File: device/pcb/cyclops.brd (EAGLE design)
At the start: 124.5 x 79.9 mm, 187 parts, among them Q1 SSM3K324, Q2 SSM3K324, Q3 SSM3K324, Q4 IRF510, U1 MCP4921, U10 ADG1201, U11 THS4281, U12 MAX4564, U13 ZXTD, U14 ZXTD, U15 OPA1664, U16 LTM8020, U2 LT1931, U3 LT1764A, U4 BD00FC0WEFJ, U5 TPS72325, U6 LT1711, U7 TLV3701, U8 ADR03, U9 LT1880

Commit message: Towards final updates for revision 3.6
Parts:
- removed D1: 1N5819, jonnew:SOD123
- added VREF<>TTL1: AS12CV, jonnew:AS12A*_SPDT
- Q1, Q2: value SSM3K324 -> NDS351AN
- U69: value SSM3K324 -> FDN352AP
- renumbered Q3 to U69
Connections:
- net OVER_CURR_PRE renamed ~OVER_CURR_PRE
- removed net OC: OC.C2, U69.D
- removed net OVER_CURR: U10.6
- new net N$16: R30.2, U69.D
- new net N$19: VCTL.1, VREF<>TTL1.P1
- net +6V: now also R29.1, U69.S; no longer R30.2
- net GND: now also OC.C2; no longer R29.1, U69.S
- net REF5.0: now also VREF<>TTL1.P3
- net VINPUT: now also VREF<>TTL1.P2; no longer VCTL.1
- net ~OVER_CURR: now also U10.6
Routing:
- net ~OVER_CURR: track 0.00 -> 18.8 mm, vias 0 -> 2
- net OVER_CURR: track 15.4 -> 0.00 mm, vias 2 -> 0
- net REF5.0: track 71.2 -> 84.3 mm
- net OC: track 12.0 -> 0.00 mm
- net N$19: track 0.00 -> 8.52 mm
- net VINPUT: track 59.3 -> 66.8 mm, vias 0 -> 1
- net GND: track 107.1 -> 104.5 mm, vias 419 -> 418
- net N$16: track 0.00 -> 2.55 mm
- net LED_ACTIVE: track 77.3 -> 75.3 mm, vias 4 -> 2
- net +6V: track 59.7 -> 61.3 mm
- net VAUX_OUT: track 46.7 -> 45.9 mm, vias 4 -> 2
- net VI: vias 2 -> 0
- net N$37: vias 0 -> 2
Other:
- board text added: "VCTL or CONT"
- board text added: "VREF or LED_ACTIVE"

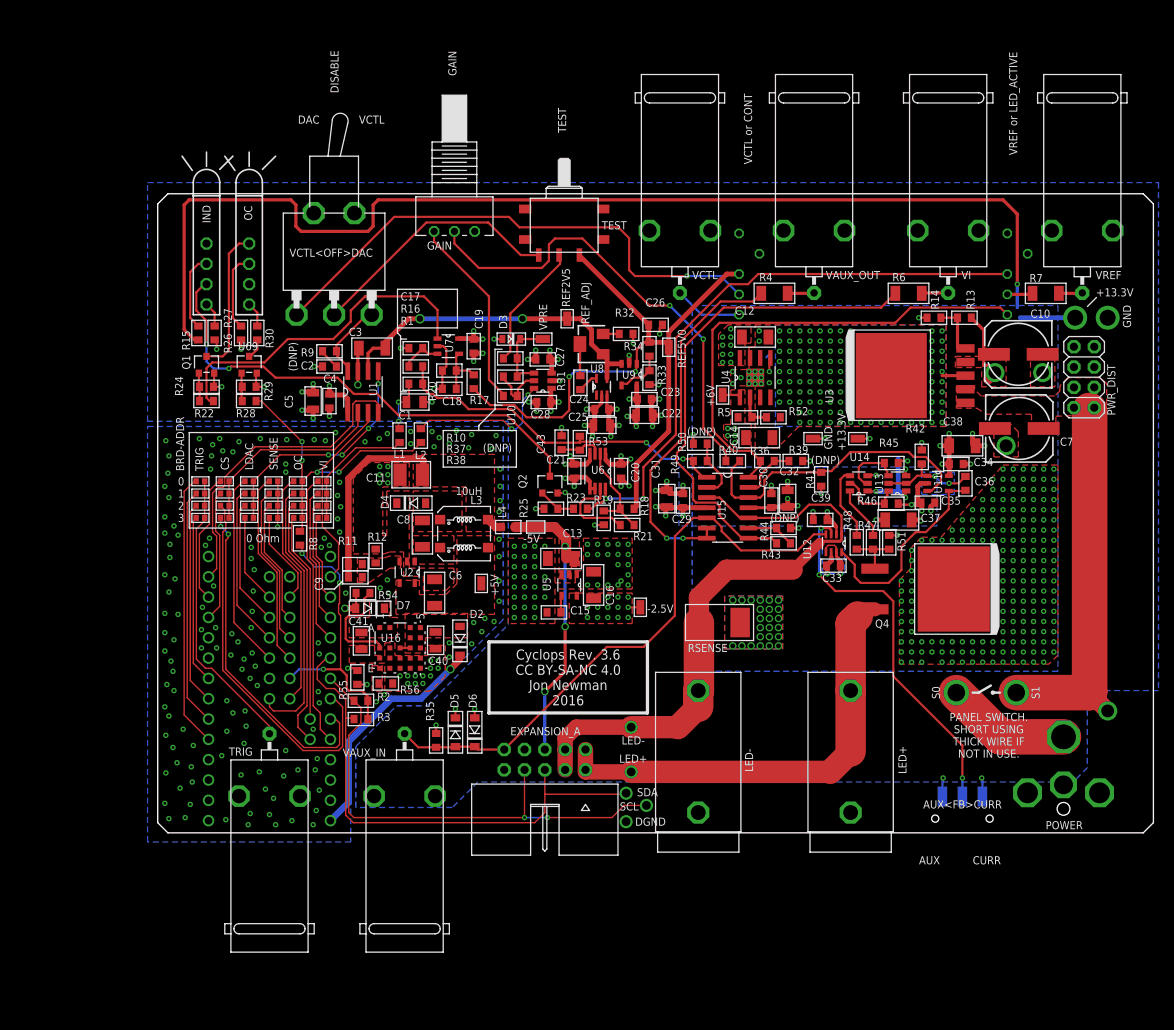
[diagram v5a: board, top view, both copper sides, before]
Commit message: Moved the LED to drain side of FET
- This prevents Vgs from dropping in nonlinear fashion as LED turns on.
  Not sure why LED was on low side to begin with.
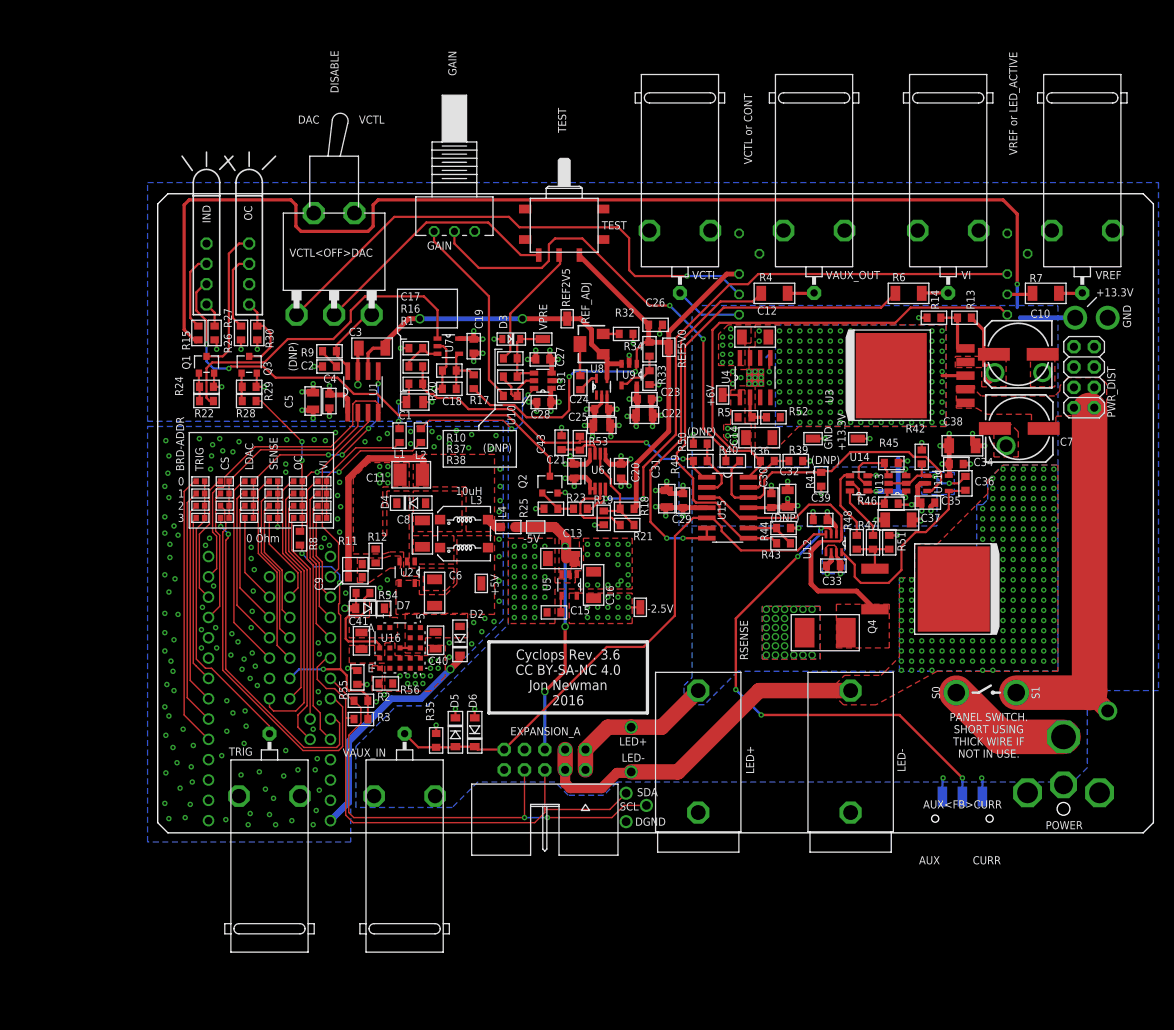
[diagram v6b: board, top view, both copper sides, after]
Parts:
- Q3: value FDN352AP -> NDS351AN
- moved LED+ 19.1 mm to (67.6, 2.54)
- moved LED- 19.1 mm to (86.6, 2.54)
- moved RSENSE 13.3 mm to (83.4, 25.0), turned to 0 degrees
- renumbered U69 to Q3, VREF<>TTL1 to VCTL<>CONT
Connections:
- removed net LED+: EXPANSION_A.1, EXPANSION_A.2, LED+.1, LED+.2, Q4.S
- removed net N$16: Q3.D, R30.2
- new net ISENSE: Q4.S, RSENSE.2, U12.1, U15.10, U15.3
- net +13.3V: now also EXPANSION_A.1, EXPANSION_A.2, LED+.1, LED+.2; no longer Q4.D
- net +6V: now also R30.2; no longer Q3.S, R29.1
- net GND: now also Q3.S, R29.1
- net LED-: now also Q4.D; no longer RSENSE.2, U12.1, U15.10, U15.3
- net N$41: now also Q3.D
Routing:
- net LED+: track 57.2 -> 0.00 mm, vias 1 -> 0
- net ISENSE: track 0.00 -> 40.0 mm
- net LED-: track 79.5 -> 45.2 mm, vias 1 -> 180
- net +13.3V: track 180.7 -> 200.3 mm, vias 207 -> 21
- net IN: track 46.5 -> 61.7 mm, vias 3 -> 5
- net N$41: track 3.11 -> 10.1 mm
- net GND: track 104.5 -> 107.3 mm, vias 418 -> 419
- net N$16: track 2.55 -> 0.00 mm
- net +6V: track 61.3 -> 59.7 mm
- net SDA: track 65.2 -> 66.0 mm
- added copper zone on layer 1, net ISENSE
- added copper zone on layer 1, net LED-
- added copper zone on layer 16, net LED-
